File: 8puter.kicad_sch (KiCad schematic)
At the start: 2 parts

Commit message: Memory Module
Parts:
- UCLK1: value (none) -> ACO-10MHz-A; footprint (none) -> Oscillator:Oscillator_DIP-14_LargePads
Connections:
- net A/~{D}: now reaches CPU1.34 (BE)
- net ~{IRQ}: now reaches CPU1.43 (~{IRQ})
- net A0 renamed ADDR0
- net A1 renamed ADDR1
- net A10 renamed ADDR10
- net A11 renamed ADDR11
- net A12 renamed ADDR12
- net A13 renamed ADDR13
- net A14 renamed ADDR14
- net A15 renamed ADDR15
- net A2 renamed ADDR2
- net A3 renamed ADDR3
- net A4 renamed ADDR4
- net A5 renamed ADDR5
- net A6 renamed ADDR6
- net A7 renamed ADDR7
- net A8 renamed ADDR8
- net A9 renamed ADDR9
- net D0 renamed DATA0
- net D1 renamed DATA1
- net D2 renamed DATA2
- net D3 renamed DATA3
- net D4 renamed DATA4
- net D5 renamed DATA5
- net D6 renamed DATA6
- net D7 renamed DATA7
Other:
- added sheet Peripheral Handler (sch/peripheral.kicad_sch)
- sheet Memory Unit ports: added CLK, CPU_A/~{D}, MEM{A[0..15]}, MEM{D[0..7]}; removed CPU_CLOCK
- note added: "Contains ROM, RAM and decode logic."
- moved on the sheet: UCLK1

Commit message: Bus control
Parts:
- added C2, C4: 1uF, symbol Device:C_Small
- added C3: (no value), symbol Device:C_Small
- added J1: (no value), symbol Connector:Jack-DC
- added U2: 74HC74, symbol 74xx:74LS74
- CPU1: footprint Package_QFP:PQFP-44_10x10mm_P0.8mm -> Package_DIP:DIP-40_W25.4mm_Socket_LongPads
- renumbered UCLK1 to CRYSTAL0
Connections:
- net VDD is gone; now on net +5V: CPU1.3 (VDD), CPU1.31 (VDD)
- net +5V: now also CRYSTAL0.14 (Vcc), C2.1, C4.1, U2.10 (~{S}), U2.13 (~{R})
- net CLOCK: now also U2.9 (Q); no longer CRYSTAL0.8 (OUT)
- net GND: now also C2.2, C3.2, C4.2, J1.2
- net ~{NMI}: now reaches CPU1.1 (~{NMI})
- net RDY: now reaches CPU1.41 (RDY)
- net ~{ABORT}: now reaches CPU1.42 (~{ABORT})
- net ADDR0 renamed A0
- net ADDR1 renamed A1
- net ADDR10 renamed A10
- net ADDR11 renamed A11
- net ADDR12 renamed A12
- net ADDR13 renamed A13
- net ADDR14 renamed A14
- net ADDR15 renamed A15
- net ADDR2 renamed A2
- net ADDR3 renamed A3
- net ADDR4 renamed A4
- net ADDR5 renamed A5
- net ADDR6 renamed A6
- net ADDR7 renamed A7
- net ADDR8 renamed A8
- net ADDR9 renamed A9
- net A/~{D} renamed BE
- net DATA0 renamed DBA0
- net DATA1 renamed DBA1
- net DATA2 renamed DBA2
- net DATA3 renamed DBA3
- net DATA4 renamed DBA4
- net DATA5 renamed DBA5
- net DATA6 renamed DBA6
- net DATA7 renamed DBA7
- new net: CRYSTAL0.8 (OUT), U2.11 (C)
- new net: U2.12 (D), U2.8 (~{Q})
- new net Power/PWR: C3.1, J1.1
- no-connect marks 0 -> 1
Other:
- added sheet Bus Control (sch/buses.kicad_sch)
- added sheet Video (sch/video.kicad_sch)
- sheet Memory Unit ports: added A[0..23], D[0..7]; removed CPU_A/~{D}, MEM{A[0..15]}, MEM{D[0..7]}
- sheet Peripheral Handler ports: added BUS_EN; removed none
- sheet Power ports: added PWR, RST; removed BOARD_IN
- note added: "MEMORY"
- note added: "SYS CLOCK"
- note removed: "Crystal Oscillator"
- moved on the sheet: CPU1, CRYSTAL0

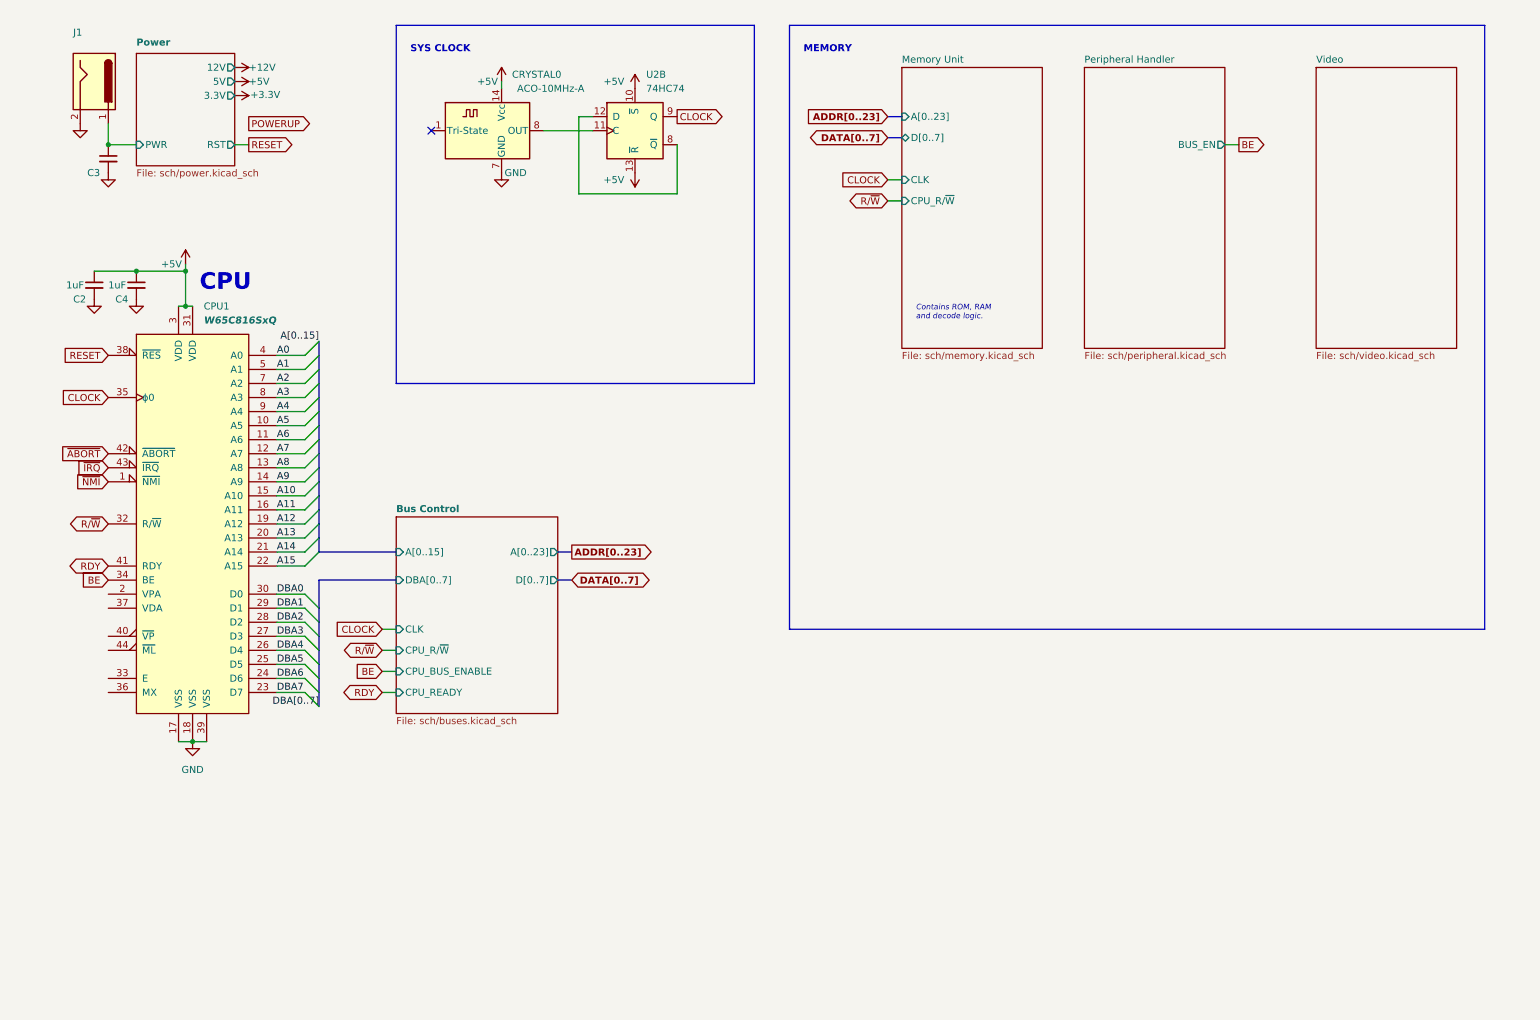
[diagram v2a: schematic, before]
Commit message: New address decoder
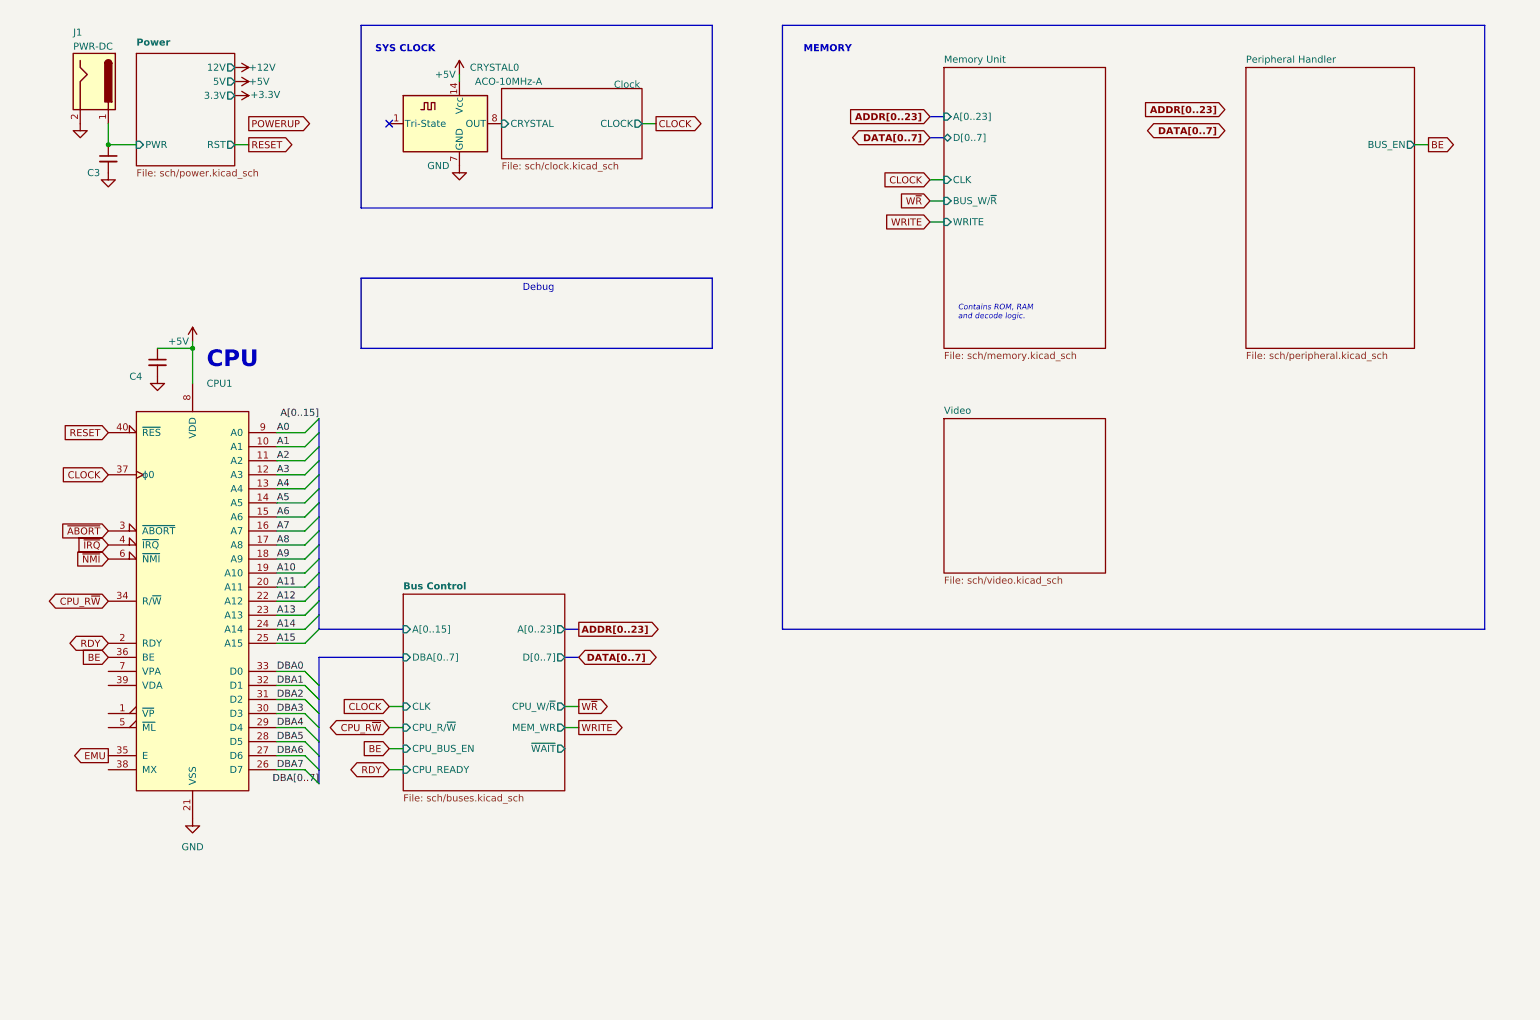
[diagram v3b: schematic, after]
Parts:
- removed C2: 1uF, symbol Device:C_Small
- removed CPU1: W65C816SxQ, Package_DIP:DIP-40_W25.4mm_Socket_LongPads, symbol 65xx:W65C816SxQ
- removed U2: 74HC74, symbol 74xx:74LS74
- added CPU1: (no value), symbol 65xx:W65C816SxP
- C4: value 1uF -> (none)
- J1: value (none) -> PWR-DC; footprint (none) -> Connector_BarrelJack:BarrelJack_CUI_PJ-063AH_Horizontal
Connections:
- net +5V: now also CPU1.8 (VDD)
- net A0: now also CPU1.9 (A0)
- net A1: now also CPU1.10 (A1)
- net A10: now also CPU1.19 (A10)
- net A11: now also CPU1.20 (A11)
- net A12: now also CPU1.22 (A12)
- net A13: now also CPU1.23 (A13)
- net A14: now also CPU1.24 (A14)
- net A15: now also CPU1.25 (A15)
- net A2: now also CPU1.11 (A2)
- net A3: now also CPU1.12 (A3)
- net A4: now also CPU1.13 (A4)
- net A5: now also CPU1.14 (A5)
- net A6: now also CPU1.15 (A6)
- net A7: now also CPU1.16 (A7)
- net A8: now also CPU1.17 (A8)
- net A9: now also CPU1.18 (A9)
- net BE: now also CPU1.36 (BE)
- net CLOCK: now also CPU1.37 (ϕ0)
- net DBA0: now also CPU1.33 (D0)
- net DBA1: now also CPU1.32 (D1)
- net DBA2: now also CPU1.31 (D2)
- net DBA3: now also CPU1.30 (D3)
- net DBA4: now also CPU1.29 (D4)
- net DBA5: now also CPU1.28 (D5)
- net DBA6: now also CPU1.27 (D6)
- net DBA7: now also CPU1.26 (D7)
- net GND: now also CPU1.21 (VSS)
- net RDY: now also CPU1.2 (RDY)
- net RESET: now also CPU1.40 (~{RES})
- net ~{ABORT}: now also CPU1.3 (~{ABORT})
- net ~{IRQ}: now also CPU1.4 (~{IRQ})
- net ~{NMI}: now also CPU1.6 (~{NMI})
- net Clock/CRYSTAL: now reaches CRYSTAL0.8 (OUT)
- new net CPU_R~{W}: CPU1.34 (R/~{W})
- new net EMU: CPU1.35 (E)
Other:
- added sheet Clock (sch/clock.kicad_sch)
- sheet Bus Control ports: added CPU_BUS_EN, CPU_W/~{R}, MEM_WR, ~{WAIT}; removed CPU_BUS_ENABLE
- sheet Memory Unit ports: added BUS_W/~{R}, WRITE; removed CPU_R/~{W}
- note added: "Debug"
- moved on the sheet: C4, CRYSTAL0

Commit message: Board layout, addr bus
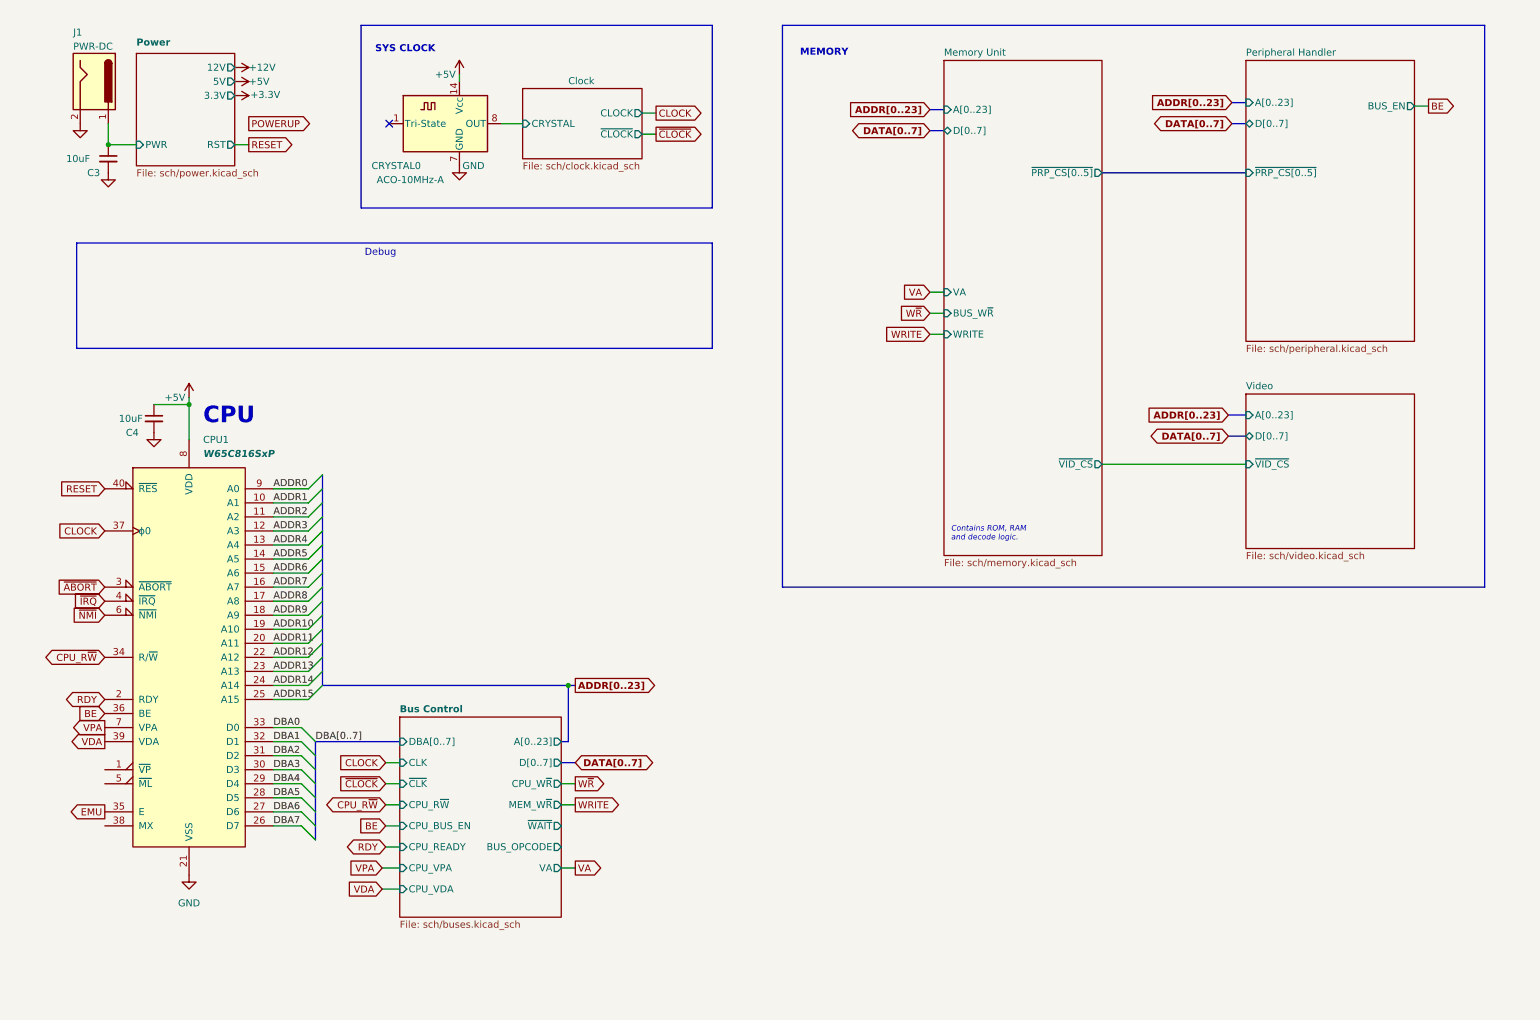
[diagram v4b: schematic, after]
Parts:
- C3: value (none) -> 10uF; footprint (none) -> Capacitor_THT:CP_Radial_D8.0mm_P5.00mm
- C4: value (none) -> 10uF; footprint (none) -> Capacitor_SMD:C_1206_3216Metric_Pad1.33x1.80mm_HandSolder
- CPU1: value (none) -> W65C816SxP; footprint (none) -> Package_DIP:DIP-40_W25.4mm_LongPads
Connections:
- net VDA: now reaches CPU1.39 (VDA)
- net VPA: now reaches CPU1.7 (VPA)
- net A0 renamed ADDR0
- net A1 renamed ADDR1
- net A10 renamed ADDR10
- net A11 renamed ADDR11
- net A12 renamed ADDR12
- net A13 renamed ADDR13
- net A14 renamed ADDR14
- net A15 renamed ADDR15
- net A2 renamed ADDR2
- net A3 renamed ADDR3
- net A4 renamed ADDR4
- net A5 renamed ADDR5
- net A6 renamed ADDR6
- net A7 renamed ADDR7
- net A8 renamed ADDR8
- net A9 renamed ADDR9
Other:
- sheet Bus Control ports: added BUS_OPCODE, CPU_R~{W}, CPU_VDA, CPU_VPA, CPU_W~{R}, MEM_W~{R}, VA, ~{CLK}; removed A[0..15], CPU_R/~{W}, CPU_W/~{R}, MEM_WR
- sheet Clock ports: added ~{CLOCK}; removed none
- sheet Memory Unit ports: added BUS_W~{R}, VA, ~{PRP_CS[0..5]}, ~{VID_CS}; removed BUS_W/~{R}, CLK
- sheet Peripheral Handler ports: added A[0..23], D[0..7], ~{PRP_CS[0..5]}; removed none
- sheet Video ports: added A[0..23], D[0..7], ~{VID_CS}; removed none
- moved on the sheet: C4, CPU1

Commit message: More routing, USB iface
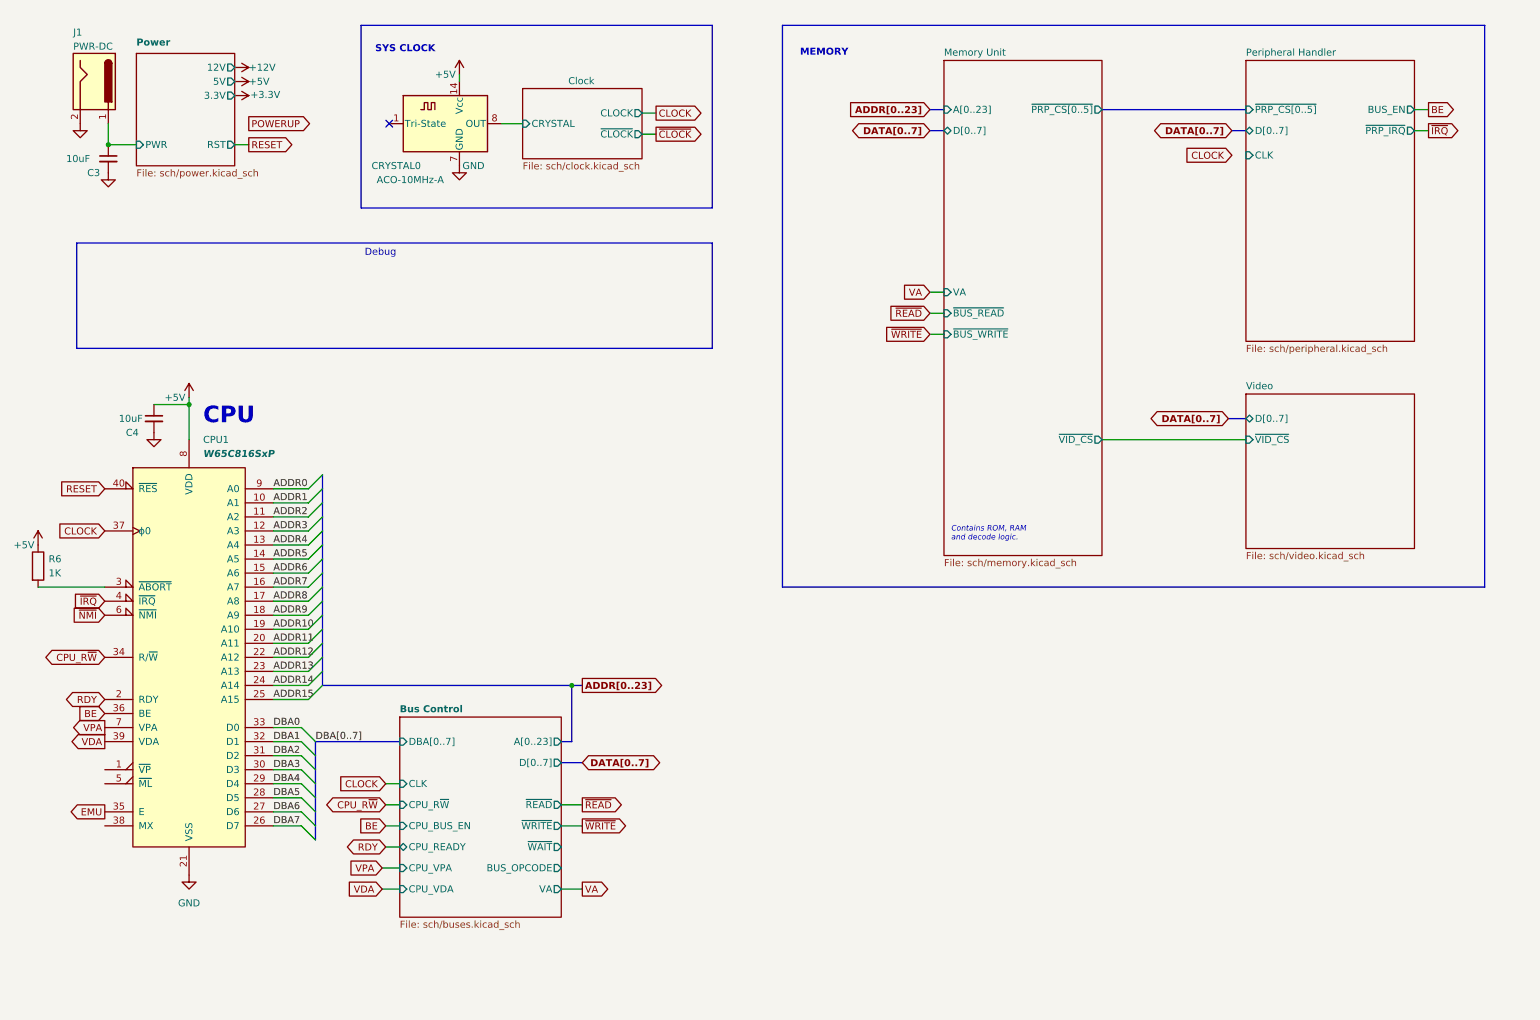
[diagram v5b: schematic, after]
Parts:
- added R6: 1K, symbol Device:R
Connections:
- net +5V: now also R6.1
- net ~{ABORT}: no longer names the net of CPU1.3 (~{ABORT})
- net ~{ABORT}: now also R6.2
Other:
- sheet Bus Control ports: added ~{READ}, ~{WRITE}; removed CPU_W~{R}, MEM_W~{R}, ~{CLK}
- sheet Memory Unit ports: added ~{BUS_READ}, ~{BUS_WRITE}; removed BUS_W~{R}, WRITE
- sheet Peripheral Handler ports: added CLK, ~{PRP_IRQ}; removed A[0..23]
- sheet Video ports: added none; removed A[0..23]

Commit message: Pivot to 6502
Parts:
- R6: footprint (none) -> Resistor_SMD:R_0603_1608Metric
